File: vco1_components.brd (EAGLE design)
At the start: 106 x 50 mm, 59 parts, among them IC1 LM13700N, Q3 2N3904, Q4 2N3904, U1 TL072_, U2 TL072_, U3 TL072_

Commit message: Massive Changes, See Readme
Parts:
- removed U$2: (no value), MusicThingModular:MOUNTING_HOLE
- added JP2, JP3: (no value), pinhead:1_05X2MM
- U$1: value THAT-340TRANSISTORS -> THAT-340; device MusicThingModular:THAT340 -> MusicThingModular:DIL14
- moved JP1 9.68 mm to (30.0, 3.17)
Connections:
- net GND: now also JP2.1, JP2.2, JP2.3, JP2.4, JP2.5, JP3.1, JP3.2, JP3.3, JP3.4, JP3.5
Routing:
- net GND: track 0.00 -> 15.2 mm
- net TRI_OUT: track 105.7 -> 94.8 mm
- net CV_B: track 19.8 -> 29.6 mm
- net LIN_FM_CV: track 82.3 -> 73.4 mm
- net CV_A: track 46.5 -> 38.6 mm
- net PWM_CV: track 18.9 -> 24.2 mm
- net N$13: track 89.0 -> 85.7 mm
- net SIN_OUT: track 79.1 -> 76.6 mm
- net PW_OUT: track 47.4 -> 45.1 mm
- net N$33: track 47.4 -> 45.3 mm
- net +12V: track 156.9 -> 154.9 mm
- net N$31: track 63.1 -> 61.1 mm
- net N$12: track 59.7 -> 58.2 mm
- net N$38: track 31.5 -> 30.0 mm
- net N$22: track 31.4 -> 30.1 mm
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
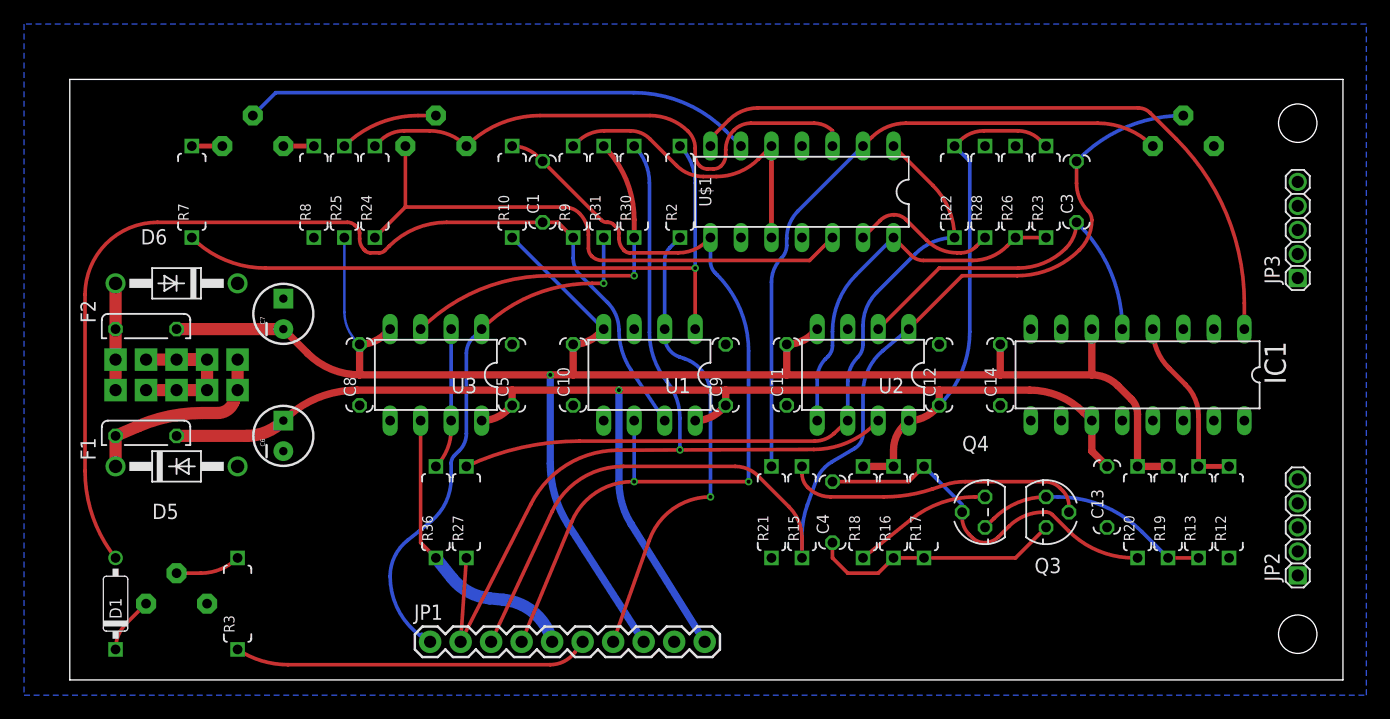
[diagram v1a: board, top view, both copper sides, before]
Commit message: Changed PCB Size, Moved Frequency Knob
Adapted PCB Boards for the (cheaper) size of 100x49mm which allows two
PCBs on one 100x100mm Panel. Frequency Pot had to be moved X -1mm
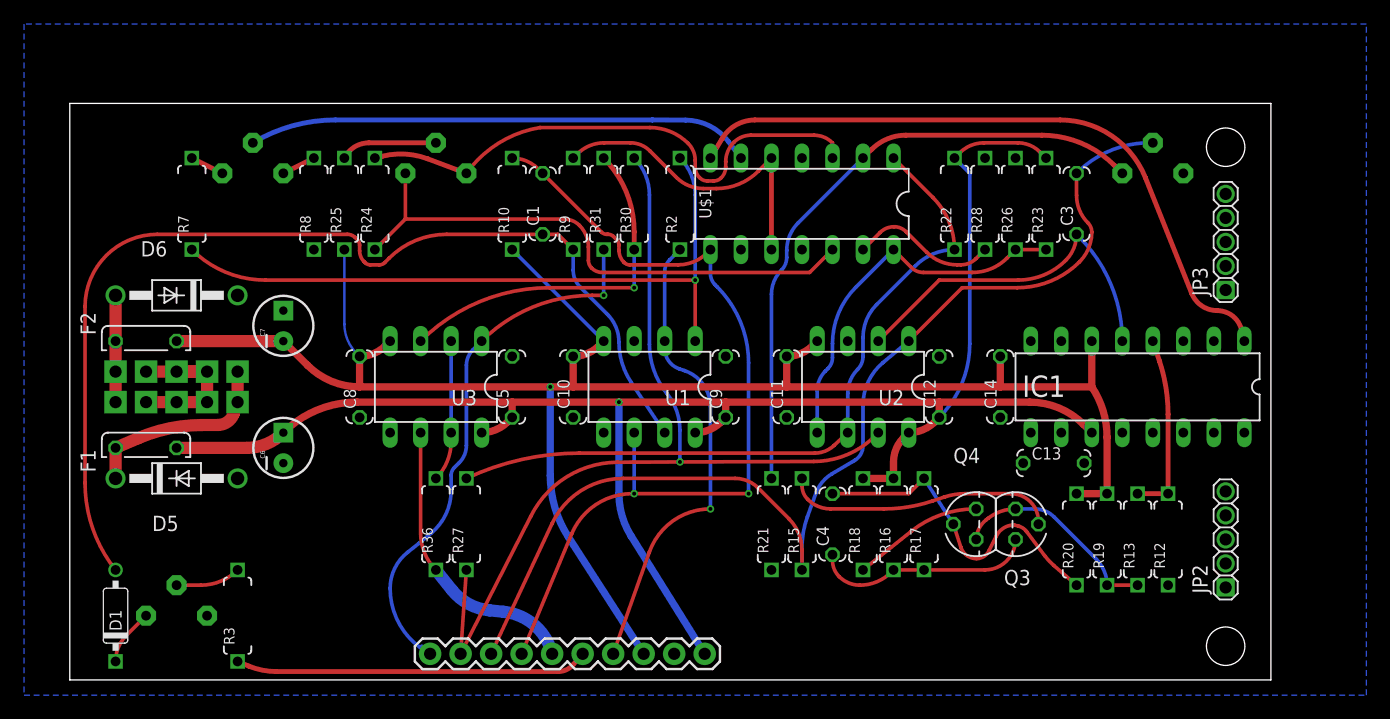
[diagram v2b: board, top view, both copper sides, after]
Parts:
- removed U$3, U$4: (no value), MusicThingModular:MOUNTING_HOLE
- moved JP2 6.08 mm to (96.2, 11.7)
- moved JP3 6.08 mm to (96.2, 36.5)
- moved R20 5.56 mm to (83.8, 11.7)
- moved R12 5.56 mm to (91.4, 11.7)
- moved R13 5.56 mm to (88.9, 11.7)
- moved R19 5.56 mm to (86.4, 11.7)
- moved C13 5.26 mm to (81.9, 18.1), turned to 0 degrees
- moved SINE_ROUND_TRIM 3.41 mm to (90.2, 42.2)
- moved Q3 2.73 mm to (78.7, 13.0)
- moved SINE_SYMMETRY 2.27 mm to (30.5, 42.2)
- moved V/OCT_TRIM 2.27 mm to (15.2, 42.2)
- moved Q4 1.24 mm to (75.5, 13.0)
- moved C1 1.00 mm to (39.4, 39.6)
- moved C10 1.00 mm to (41.9, 24.4)
- moved C11 1.00 mm to (59.7, 24.4)
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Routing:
- net +12V: track 154.9 -> 150.5 mm
- net N$27: track 31.2 -> 28.0 mm
- net N$25: track 21.2 -> 18.1 mm
- net N$24: track 25.4 -> 22.5 mm
- net TRI_OUT: track 94.8 -> 92.0 mm
- net N$12: track 58.2 -> 55.5 mm
- net N$30: track 19.9 -> 17.7 mm
- net N$26: track 54.4 -> 52.3 mm
- net N$34: track 47.9 -> 46.7 mm
- net N$28: track 11.6 -> 10.9 mm
- net N$10: track 42.6 -> 42.0 mm
- net -12V: track 156.4 -> 155.9 mm
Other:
- board size 106 x 50 mm -> 100 x 48 mm
